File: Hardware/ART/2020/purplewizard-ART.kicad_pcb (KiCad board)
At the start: 2 copper layers, 92.5 x 151 mm, 22 parts, among them J1 SDA, J2 SCL, J3 ART Expansion, J4 EXP1, J5 EXP2, J6 3v3, J7 GND

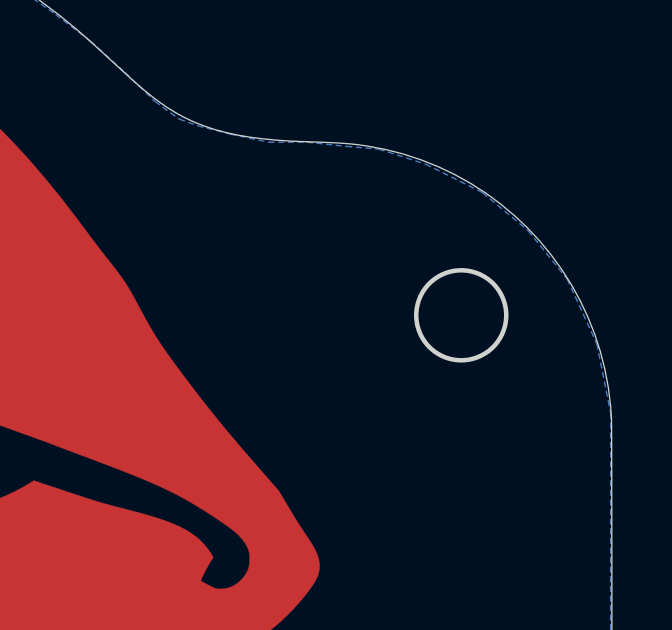
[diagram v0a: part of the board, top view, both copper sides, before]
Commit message: Adding PogoProto jig Fixed upper right hole being off 3/4 of a millimeter Added some pads for USB and added some vias to help pogo pin alignment
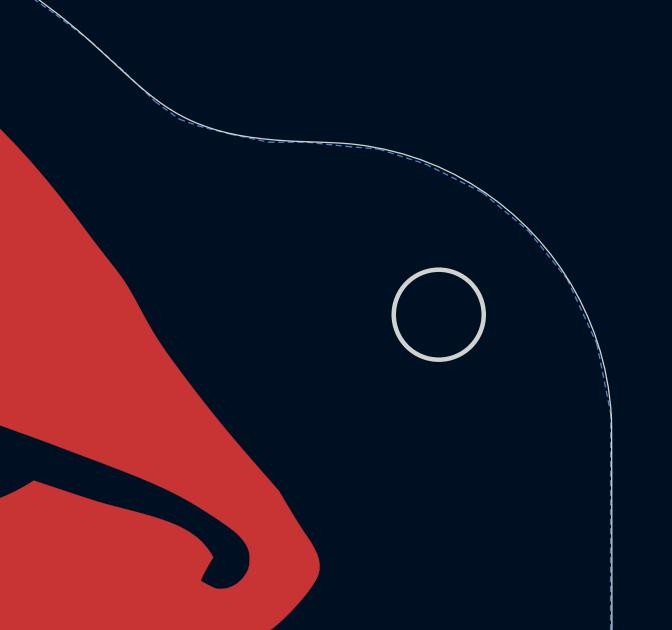
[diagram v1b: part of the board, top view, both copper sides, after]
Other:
- rule pad_to_mask_clearance: 0.2 -> 0
